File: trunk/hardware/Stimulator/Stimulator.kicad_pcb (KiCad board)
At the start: 2 copper layers, 58.4 x 31.8 mm, 101 parts, among them P1 CONN_1, P10 CONN_1, P11 CONN_1, P12 CONN_1, P13 CONN_1, P14 CONN_1, P15 CONN_1, P16 CONN_1, P17 CONN_1, P18 CONN_1, P19 CONN_1, P2 CONN_10X2, P20 CONN_1, P21 CONN_1, P22 CONN_1, P23 CONN_1, P24 CONN_1, P25 CONN_1, P26 CONN_1, P27 CONN_1, P28 CONN_1, P29 CONN_1, P3 CONN_1, P30 CONN_1, P31 CONN_1, P32 CONN_1, P33 CONN_1, P34 CONN_1, P35 CONN_1, P36 CONN_1, P37 CONN_10X2, P38 CONN_1, P39 CONN_1, P4 CONN_1, P40 CONN_1, P41 CONN_1, P42 CONN_1, P43 CONN_1, P44 CONN_1, P45 CONN_1, P46 CONN_1, P47 CONN_1, P48 CONN_1, P49 CONN_1, P5 CONN_1, P50 CONN_1, P51 CONN_1, P52 CONN_1, P53 CONN_1, P54 CONN_1, P55 CONN_1, P56 CONN_1, P57 CONN_1, P6 CONN_1, P7 CONN_1, P8 CONN_1, P9 CONN_1, Q1 2N7002, Q2 2N7002, Q3 2N7002, Q4 2N7002, U1 MCP42010, U2 MCP42010, U3 MCP42010, U4 MCP42010

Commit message: 2N7002KCT-ND
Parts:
- added C1: 1uF, SM0805, B.Cu at (111.1, 85.1)
- added C16: 1uF, SM0805, B.Cu at (193.7, 85.1)
- added C17: 1uF, SM0805, B.Cu at (193.7, 78.7)
- added C18: 1uF, SM0805, B.Cu at (191.1, 83.2)
- added C19: 1uF, SM0805, B.Cu at (192.4, 74.3)
- added C2: 1uF, SM0805, B.Cu at (111.1, 78.7)
- added C20: 1uF, SM0805, B.Cu at (191.1, 76.8)
- added C21: 1uF, SM0805, B.Cu at (191.1, 67.3)
- added C22: 1uF, SM0805, B.Cu at (193.7, 67.3)
- added C3: 1uF, SM0805, B.Cu at (108.6, 82.5)
- added C4: 1uF, SM0805, B.Cu at (109.9, 74.3)
- added C5: 1uF, SM0805, B.Cu at (108.6, 76.8)
- added C6: 1uF, SM0805, B.Cu at (108.6, 67.3)
- added C7: 1uF, SM0805, B.Cu at (111.1, 67.3)
- added D1: ECU PWR, LED-0805, F.Cu at (119.4, 88.3)
- added D2: STIM PWR, LED-0805, F.Cu at (185.4, 60.3)
- added P1: CONN_1, PIN_ARRAY_1, F.Cu at (103.5, 64.8)
- added P13: CONN_1, PIN_ARRAY_1, F.Cu at (117.5, 85.7)
- added P15: CONN_10, SIL-10, F.Cu at (121.9, 73.7)
- added P2: CONN_1, PIN_ARRAY_1, F.Cu at (116.2, 64.8)
- added P24: CONN_10, SIL-10, F.Cu at (129.5, 73.7)
- added P3: CONN_1, PIN_ARRAY_1, F.Cu at (103.5, 67.3)
- added P4: CONN_1, PIN_ARRAY_1, F.Cu at (116.2, 67.3)
- added P40: TEST, SIL-2, F.Cu at (148.6, 62.2)
- added P5: CONN_1, PIN_ARRAY_1, F.Cu at (103.5, 69.8)
- added P6: CONN_1, PIN_ARRAY_1, F.Cu at (116.2, 69.8)
- added P64: CONN_10, SIL-10, F.Cu at (172.7, 76.2)
- added P7: CONN_1, PIN_ARRAY_1, F.Cu at (107.3, 59.7)
- added P71: CONN_1, PIN_ARRAY_1, F.Cu at (186.1, 64.8)
- added P72: CONN_1, PIN_ARRAY_1, F.Cu at (198.8, 64.8)
- added P73: CONN_1, PIN_ARRAY_1, F.Cu at (186.1, 67.3)
- added P74: CONN_1, PIN_ARRAY_1, F.Cu at (198.8, 67.3)
- added P75: CONN_10, SIL-10, F.Cu at (180.3, 76.2)
- added P76: CONN_1, PIN_ARRAY_1, F.Cu at (186.1, 69.8)
- added P77: CONN_1, PIN_ARRAY_1, F.Cu at (198.8, 69.8)
- added P78: CONN_1, PIN_ARRAY_1, F.Cu at (189.9, 59.7)
- added P79: CONN_1, PIN_ARRAY_1, F.Cu at (194.9, 59.7)
- added P8: CONN_1, PIN_ARRAY_1, F.Cu at (112.4, 59.7)
- added R1: 10k, SM0805, B.Cu at (108.6, 63.5)
- added R2: 10k, SM0805, B.Cu at (111.1, 63.5)
- added R3: 700R, SM0805, F.Cu at (117.5, 88.3)
- added R32: 700R, SM0805, F.Cu at (182.9, 60.3)
- added R33: 10k, SM0805, B.Cu at (191.1, 63.5)
- added R34: 10k, SM0805, B.Cu at (193.7, 63.5)
- added U1: MAX232, DIP-20__300_ELL, F.Cu at (109.9, 76.2)
- added U6: MAX232, DIP-20__300_ELL, F.Cu at (192.4, 76.2)
- C10: renamed from C1; footprint SMD_Packages:SM0805 -> SM0805
- C11: renamed from C2; footprint SMD_Packages:SM0805 -> SM0805
- C12: renamed from C3; footprint SMD_Packages:SM0805 -> SM0805
- C13: renamed from C8; footprint SMD_Packages:SM0805 -> SM0805
- C14: renamed from C6; footprint SMD_Packages:SM0805 -> SM0805
- C15: renamed from C7; footprint SMD_Packages:SM0805 -> SM0805
- C8: renamed from C4; footprint SMD_Packages:SM0805 -> SM0805
- C9: renamed from C5; footprint SMD_Packages:SM0805 -> SM0805
- P10: renamed from P39; footprint Stimulator:1PIN_A -> PIN_ARRAY_1
- P11: renamed from P40; footprint Stimulator:1PIN_A -> PIN_ARRAY_1
- P12: renamed from P41; footprint Stimulator:1PIN_A -> PIN_ARRAY_1
- P14: renamed from P42; footprint Stimulator:1PIN_A -> PIN_ARRAY_1
- P16: renamed from P43; footprint Stimulator:1PIN_A -> PIN_ARRAY_1
- P17: renamed from P44; footprint Stimulator:1PIN_A -> PIN_ARRAY_1
- P18: renamed from P1; footprint Stimulator:1PIN_A -> PIN_ARRAY_1
- P20, P21, P22: footprint Stimulator:1PIN_A -> PIN_ARRAY_1
- P23: renamed from P27; value CONN_1 -> TEST; footprint Stimulator:1PIN_A -> SIL-2
- P25: renamed from P57; value CONN_1 -> TEST; footprint Stimulator:1PIN_A -> SIL-2
- P26: renamed from P3; footprint Stimulator:1PIN_A -> PIN_ARRAY_1
- P27: renamed from P4; footprint Stimulator:1PIN_A -> PIN_ARRAY_1
- P28: renamed from P5; footprint Stimulator:1PIN_A -> PIN_ARRAY_1
- P29: renamed from P6; footprint Stimulator:1PIN_A -> PIN_ARRAY_1
- P30: renamed from P7; footprint Stimulator:1PIN_A -> PIN_ARRAY_1
- P31: renamed from P52; footprint Stimulator:1PIN_A -> PIN_ARRAY_1
- P32: renamed from P55; footprint Stimulator:1PIN_A -> PIN_ARRAY_1
- P33: renamed from P45; footprint Stimulator:1PIN_A -> PIN_ARRAY_1
- P34: renamed from P8; footprint Stimulator:1PIN_A -> PIN_ARRAY_1
- P35: renamed from P9; footprint Stimulator:1PIN_A -> PIN_ARRAY_1
- P36: renamed from P56; footprint Stimulator:1PIN_A -> PIN_ARRAY_1
- P37: renamed from P46; footprint Stimulator:1PIN_A -> PIN_ARRAY_1
- P38: renamed from P47; footprint Stimulator:1PIN_A -> PIN_ARRAY_1
- P39: renamed from P48; footprint Stimulator:1PIN_A -> PIN_ARRAY_1
- P41: renamed from P28; footprint Stimulator:1PIN_A -> PIN_ARRAY_1
- P42: renamed from P29; footprint Stimulator:1PIN_A -> PIN_ARRAY_1
- P43: renamed from P30; footprint Stimulator:1PIN_A -> PIN_ARRAY_1
- P44: renamed from P31; footprint Stimulator:1PIN_A -> PIN_ARRAY_1
- P45: renamed from P36; footprint Stimulator:1PIN_A -> PIN_ARRAY_1
- P46: renamed from P23; footprint Stimulator:1PIN_A -> PIN_ARRAY_1
- P47: renamed from P24; footprint Stimulator:1PIN_A -> PIN_ARRAY_1
- P48: renamed from P25; footprint Stimulator:1PIN_A -> PIN_ARRAY_1
- P49: renamed from P26; footprint Stimulator:1PIN_A -> PIN_ARRAY_1
- P50: renamed from P10; footprint Stimulator:1PIN_A -> PIN_ARRAY_1
- P51: renamed from P11; footprint Stimulator:1PIN_A -> PIN_ARRAY_1
- P52: renamed from P12; footprint Stimulator:1PIN_A -> PIN_ARRAY_1
- P53: renamed from P49; footprint Stimulator:1PIN_A -> PIN_ARRAY_1
- P54: renamed from P13; footprint Stimulator:1PIN_A -> PIN_ARRAY_1
- P55: renamed from P53; footprint Stimulator:1PIN_A -> PIN_ARRAY_1
- P56: renamed from P14; footprint Stimulator:1PIN_A -> PIN_ARRAY_1
- P57: renamed from P15; footprint Stimulator:1PIN_A -> PIN_ARRAY_1
- P58: renamed from P16; footprint Stimulator:1PIN_A -> PIN_ARRAY_1
- P59: renamed from P17; footprint Stimulator:1PIN_A -> PIN_ARRAY_1
- P60: renamed from P18; footprint Stimulator:1PIN_A -> PIN_ARRAY_1
- P61: renamed from P19; footprint Stimulator:1PIN_A -> PIN_ARRAY_1
- P62: renamed from P50; footprint Stimulator:1PIN_A -> PIN_ARRAY_1
- P63: renamed from P51; footprint Stimulator:1PIN_A -> PIN_ARRAY_1
- P65: renamed from P32; footprint Stimulator:1PIN_A -> PIN_ARRAY_1
- P66: renamed from P33; footprint Stimulator:1PIN_A -> PIN_ARRAY_1
- P67: renamed from P34; footprint Stimulator:1PIN_A -> PIN_ARRAY_1
- P68: renamed from P35; footprint Stimulator:1PIN_A -> PIN_ARRAY_1
- P69: renamed from P54; footprint Stimulator:1PIN_A -> PIN_ARRAY_1
- P9: renamed from P38; footprint Stimulator:1PIN_A -> PIN_ARRAY_1
- Q1, Q2, Q3, Q4: footprint Transistors_SMD:sot23 -> sot23
- R10: renamed from R3; footprint SMD_Packages:SM0805 -> SM0805
- R11: renamed from R4; footprint SMD_Packages:SM0805 -> SM0805
- R12: renamed from R5; footprint SMD_Packages:SM0805 -> SM0805
- R13: renamed from R6; footprint SMD_Packages:SM0805 -> SM0805
- R14: renamed from R25; footprint SMD_Packages:SM0805 -> SM0805
- R15: renamed from R26; footprint SMD_Packages:SM0805 -> SM0805
- R16: renamed from R21; footprint SMD_Packages:SM0805 -> SM0805
- R17: renamed from R22; footprint SMD_Packages:SM0805 -> SM0805
- R18: renamed from R7; footprint SMD_Packages:SM0805 -> SM0805
- R19: renamed from R8; footprint SMD_Packages:SM0805 -> SM0805
- R20: renamed from R9; footprint SMD_Packages:SM0805 -> SM0805
- R21: renamed from R10; footprint SMD_Packages:SM0805 -> SM0805
- R22: renamed from R11; footprint SMD_Packages:SM0805 -> SM0805
- R23: renamed from R12; footprint SMD_Packages:SM0805 -> SM0805
- R24: renamed from R27; footprint SMD_Packages:SM0805 -> SM0805
- R25: renamed from R28; footprint SMD_Packages:SM0805 -> SM0805
- R26: renamed from R15; footprint SMD_Packages:SM0805 -> SM0805
- R27: renamed from R16; footprint SMD_Packages:SM0805 -> SM0805
- R28: renamed from R19; footprint SMD_Packages:SM0805 -> SM0805
- R29: renamed from R20; footprint SMD_Packages:SM0805 -> SM0805
- R30: renamed from R23; footprint SMD_Packages:SM0805 -> SM0805
- R31: renamed from R24; footprint SMD_Packages:SM0805 -> SM0805
- R4: renamed from R13; footprint SMD_Packages:SM0805 -> SM0805
- R5: renamed from R14; footprint SMD_Packages:SM0805 -> SM0805
- R6: renamed from R17; footprint SMD_Packages:SM0805 -> SM0805
- R7: renamed from R18; footprint SMD_Packages:SM0805 -> SM0805
- R8: renamed from R1; footprint SMD_Packages:SM0805 -> SM0805
- R9: renamed from R2; footprint SMD_Packages:SM0805 -> SM0805
- U2: renamed from U1; footprint SOIC_Packages:SOIC-14_Narrow -> SO14N
- U3: renamed from U2; footprint SOIC_Packages:SOIC-14_Narrow -> SO14N
- U4: renamed from U3; footprint SOIC_Packages:SOIC-14_Narrow -> SO14N
- U5: renamed from U4; footprint SOIC_Packages:SOIC-14_Narrow -> SO14N
- moved P12 14.5 mm to (153.7, 74.9), turned to 180 degrees
- moved P31 5.12 mm to (150.5, 68.6)
- moved P23 2.84 mm to (132.1, 86.4), turned to 270 degrees
- moved P18 1.91 mm to (132.7, 61.0), turned to 0 degrees
- moved P36 1.91 mm to (132.7, 74.9), turned to 180 degrees
- moved P37 1.91 mm to (135.3, 74.9), turned to 180 degrees
- moved P52 1.91 mm to (135.3, 72.4)
- moved P54 1.91 mm to (132.7, 63.5)
- moved P25 1.80 mm to (151.1, 62.2), turned to 90 degrees
- moved P17 1.27 mm to (170.2, 61.0)
- moved P26 1.27 mm to (153.7, 63.5), turned to 270 degrees
- moved P55 1.27 mm to (170.2, 63.5), turned to 270 degrees
- moved R4 0.63 mm to (170.8, 79.4)
- moved R13 0.38 mm to (147.7, 66.0)
- turned P10 to 180 degrees
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- renumbered P2 to P19, P37 to P70
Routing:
- net GND: track 40.3 -> 59.5 mm, vias 4 -> 10
- net /Vdpu_14: track 44.4 -> 33.0 mm
- net /Vdpu_58: track 42.3 -> 32.5 mm
- net /Vd: track 109.2 -> 100.3 mm
- net N-0000052: track 0.00 -> 7.19 mm
- net N-0000050: track 0.00 -> 7.19 mm
- net N-0000056: track 0.00 -> 7.19 mm
- net N-0000055: track 0.00 -> 7.19 mm
- net N-0000074: track 0.00 -> 5.77 mm
- net N-0000039: track 0.00 -> 5.47 mm
- net N-0000051: track 0.00 -> 5.18 mm
- net N-0000057: track 0.00 -> 5.18 mm
- net N-0000053: track 0.00 -> 5.18 mm
- net N-0000043: track 0.00 -> 5.18 mm
- net /MOSI: track 52.8 -> 48.5 mm
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- added copper zone on F.Cu, net /Vd
- removed copper zone on F.Cu, net GND
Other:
- board size 58.4 x 31.8 mm -> 101.6 x 32.4 mm
- board text added: "DanMoto Stimulator June 2014 R0.2"
- board text removed: "DanMoto Stimulator June 2014"

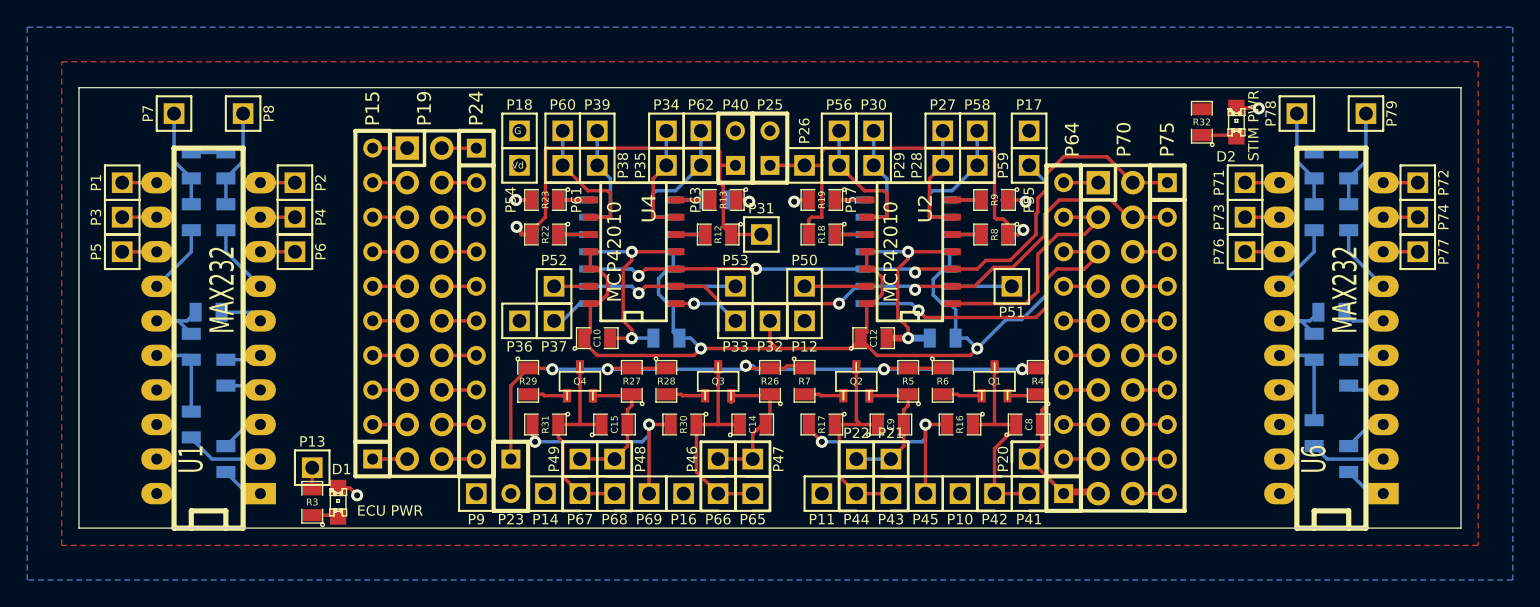
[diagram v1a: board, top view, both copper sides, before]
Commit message: 
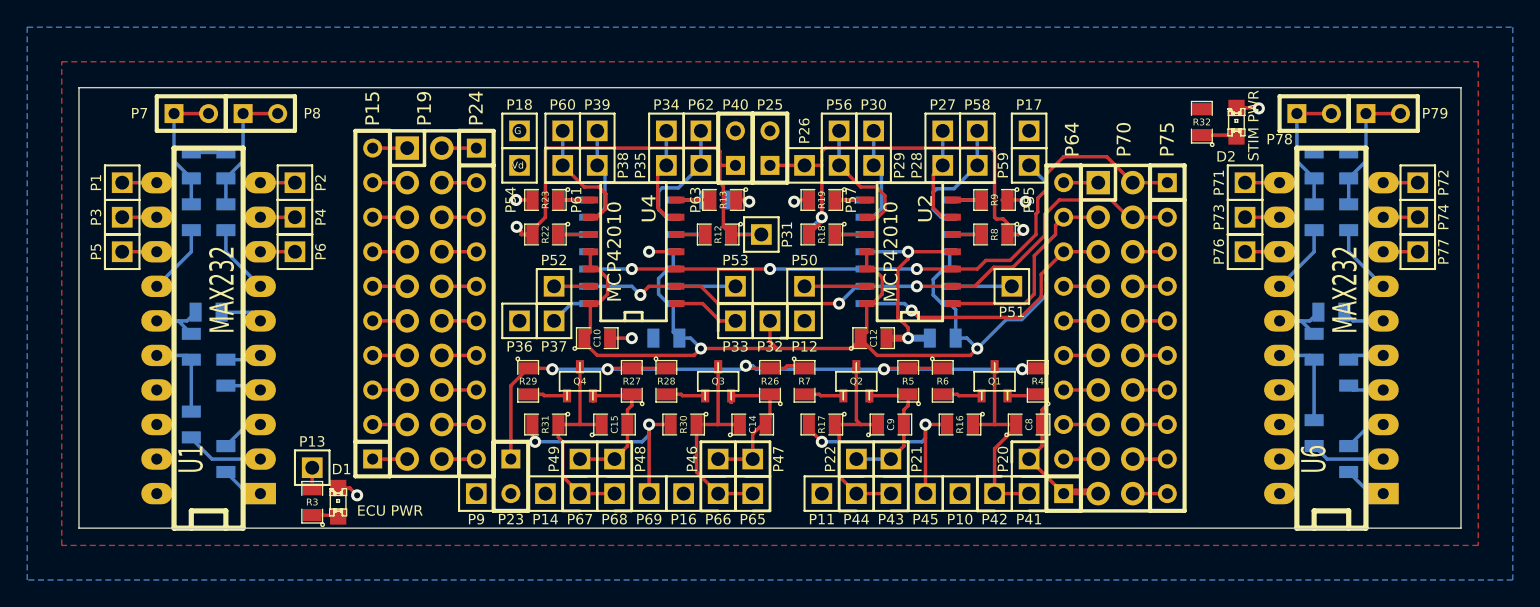
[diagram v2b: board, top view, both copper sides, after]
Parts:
- P7, P78, P79, P8: value CONN_1 -> TEST; footprint PIN_ARRAY_1 -> SIL-2
- moved P79 1.27 mm to (196.2, 59.7), turned to 0 degrees
- moved P8 1.27 mm to (113.7, 59.7), turned to 0 degrees
- moved P7 1.27 mm to (108.6, 59.7), turned to 0 degrees
- moved P78 1.27 mm to (191.1, 59.7), turned to 0 degrees
- turned P21 to 270 degrees
- turned P22 to 90 degrees
- turned P31 to 270 degrees
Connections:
- C21 pad 2: N-0000055 (its old number) -> /VR2-O1
- C22 pad 2: N-0000056 (its old number) -> /VR2-O2
- C6 pad 2: N-0000050 (its old number) -> /VR1-O1
- C7 pad 2: N-0000052 (its old number) -> /VR1-O2
- P1 pad 1: N-0000073 (its old number) -> /VR1_i1
- P2 pad 1: N-0000076 (its old number) -> /VR1_i2
- P7 pad 1: N-0000050 (its old number) -> /VR1-O1
- P71 pad 1: N-0000047 (its old number) -> /VR2_i1
- P72 pad 1: N-0000046 (its old number) -> /VR2_i2
- P78 pad 1: N-0000055 (its old number) -> /VR2-O1
- P79 pad 1: N-0000056 (its old number) -> /VR2-O2
- P8 pad 1: N-0000052 (its old number) -> /VR1-O2
- R1 pad 1: N-0000050 (its old number) -> /VR1-O1
- R2 pad 1: N-0000052 (its old number) -> /VR1-O2
- R33 pad 1: N-0000055 (its old number) -> /VR2-O1
- R34 pad 1: N-0000056 (its old number) -> /VR2-O2
- U1 pad 10: N-0000076 (its old number) -> /VR1_i2
- U1 pad 11: N-0000073 (its old number) -> /VR1_i1
- U6 pad 10: N-0000046 (its old number) -> /VR2_i2
- U6 pad 11: N-0000047 (its old number) -> /VR2_i1
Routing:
- net GND: track 59.5 -> 48.8 mm
- net /VR2-O2: track 0.00 -> 9.73 mm
- net /VR1-O2: track 0.00 -> 9.73 mm
- net /VR1-O1: track 0.00 -> 9.73 mm
- net /VR2-O1: track 0.00 -> 9.73 mm
- net N-0000052 (its old number): track 7.19 -> 0.00 mm
- net N-0000050 (its old number): track 7.19 -> 0.00 mm
- net N-0000056 (its old number): track 7.19 -> 0.00 mm
- net N-0000055 (its old number): track 7.19 -> 0.00 mm
- net /CS_12: track 18.2 -> 15.3 mm
- net N-0000073 (its old number): track 2.54 -> 0.00 mm
- net /VR1_i1: track 0.00 -> 2.54 mm
- net N-0000076 (its old number): track 2.54 -> 0.00 mm
- net N-0000047 (its old number): track 2.54 -> 0.00 mm
- net N-0000046 (its old number): track 2.54 -> 0.00 mm
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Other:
- board text added: "For rusEFI DanMoto Stimulator June 2014 R0.2 http://code.google.com/p/daecu"
- board text added: "IN_1"
- board text added: "IN_2"
- board text added: "IN_3"
- board text added: "IN_4"
- board text added: "PA8/IN 1"
- board text added: "VR1_O1"
- board text added: "VR1_O2"
- board text added: "VR1_i1"
- board text added: "VR1_i2"
- board text added: "VR2_O2"
- board text removed: "DanMoto Stimulator June 2014 R0.2"
- board text removed: "IN"
- board text removed: "PA8"

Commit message: 
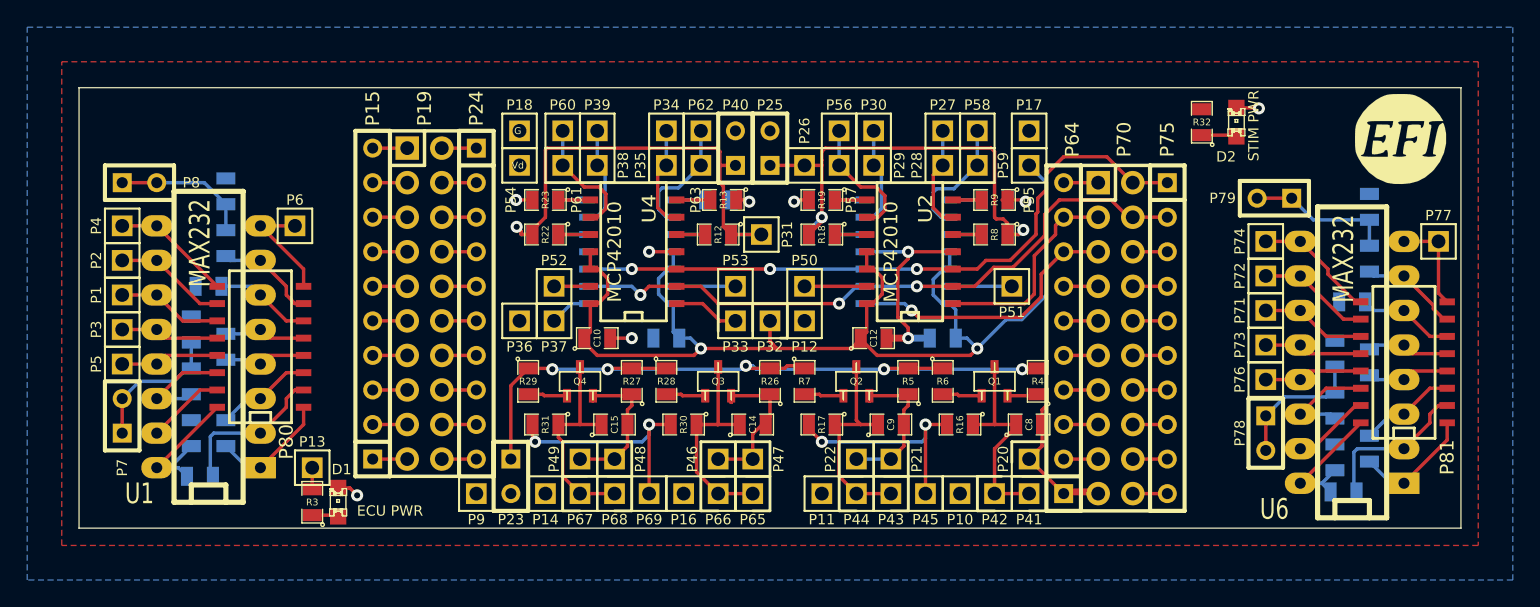
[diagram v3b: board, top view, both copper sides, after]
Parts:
- added G***: LOGO, LOGO, F.Cu at (197.5, 61.6)
- added G***: LOGO_F, LOGO_F, B.Cu at (197.5, 61.6)
- added P80: DIL16, SO16N, F.Cu at (113.7, 76.8)
- added P81: DIL16, SO16N, F.Cu at (197.7, 78.0)
- U1, U6: footprint DIP-20__300_ELL -> DIP-16__300_ELL
- moved P78 23.8 mm to (187.6, 83.2), turned to 270 degrees
- moved P7 22.8 mm to (103.5, 81.9), turned to 90 degrees
- moved C21 13.9 mm to (192.7, 81.2)
- moved P2 13.9 mm to (103.5, 70.5), turned to 90 degrees
- moved R33 13.9 mm to (192.7, 77.3)
- moved P72 13.1 mm to (187.6, 71.6), turned to 90 degrees
- moved P4 12.7 mm to (103.5, 67.9), turned to 90 degrees
- moved C6 12.1 mm to (108.6, 79.4)
- moved R1 12.1 mm to (108.6, 75.6)
- moved P74 11.3 mm to (187.6, 69.1), turned to 90 degrees
- moved P8 10.2 mm to (104.8, 64.8)
- moved P79 10.1 mm to (188.2, 65.9), turned to 180 degrees
- moved P71 9.52 mm to (187.6, 74.2)
- moved P76 9.52 mm to (187.6, 79.2)
- moved P73 9.52 mm to (187.6, 76.7)
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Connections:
- net N-0000047 renamed /U6-01
- net N-0000048 renamed /U6-03
- net N-0000049 renamed /U6-04
- net N-0000050 renamed /U6-05
- net N-0000051 renamed /U6-02
- net N-0000059 renamed /U6-09
- net N-0000062 renamed /U6-12
- net N-0000063 renamed /U6-14
- net N-0000065 renamed /U1-12
- net N-0000066 renamed /U1-09
- net N-0000071 renamed /U1-07
- net N-0000072 renamed /U1-01
- net N-0000073 renamed /U1-02
- net N-0000074 renamed /U1-03
- net N-0000075 renamed /U1-04
- net N-0000076 renamed /U1-05
- net N-0000079 renamed /U1-13
- net N-0000080 renamed /U1-14
- C19 pad 1: N-0000052 (its old number) -> /U6-06
- C22 pad 1: N-0000058 (its old number) -> /U6-07
- C4 pad 1: N-0000077 (its old number) -> /U1-06
- P6 pad 1: N-0000078 (its old number) -> /U1-08
- P76 pad 1: N-0000055 (its old number) -> /U6-13
- P77 pad 1: N-0000054 (its old number) -> /U6-08
- U1 pad 6: N-0000077 (its old number) -> /U1-06
- U1 pad 8: N-0000078 (its old number) -> /U1-08
- U6 pad 13: N-0000055 (its old number) -> /U6-13
- U6 pad 6: N-0000052 (its old number) -> /U6-06
- U6 pad 7: N-0000058 (its old number) -> /U6-07
- U6 pad 8: N-0000054 (its old number) -> /U6-08
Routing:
- net /Vd: track 100.3 -> 108.8 mm
- net /U1-08: track 0.00 -> 8.30 mm
- net /U6-07: track 0.00 -> 7.31 mm
- net /U6-13: track 0.00 -> 7.25 mm
- net /U6-08: track 0.00 -> 7.25 mm
- net /U1-06: track 0.00 -> 7.08 mm
- net /U6-06: track 0.00 -> 7.08 mm
- net /U6-09: track 2.54 -> 9.05 mm
- net /U1-09: track 2.54 -> 8.83 mm
- net /U6-02: track 5.47 -> 11.7 mm
- net /U1-02: track 5.77 -> 11.7 mm
- net /VR1_i2: track 2.54 -> 8.30 mm
- net /U1-01: track 3.20 -> 8.96 mm
- net /VR2_i2: track 2.54 -> 8.30 mm
- net /U6-01: track 3.20 -> 8.96 mm
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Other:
- board text added: "VR2_O1"

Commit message: updates
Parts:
- added P82: CONN_1, PIN_ARRAY_1, F.Cu at (114.9, 88.3)
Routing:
- net N-0000065: track 1.59 -> 5.18 mm
